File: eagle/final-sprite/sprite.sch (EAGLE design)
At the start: 62 parts, among them J1 M20-7910442R, U1 CC430F513X, U2 LSM9DS1, U4 DRV8837, U5 ADP5092, U6 DRV8837, U7 DRV8837, X1 SPRITEPIN_SPRITE_PIN, X2 SPRITEPIN_SPRITE_PIN

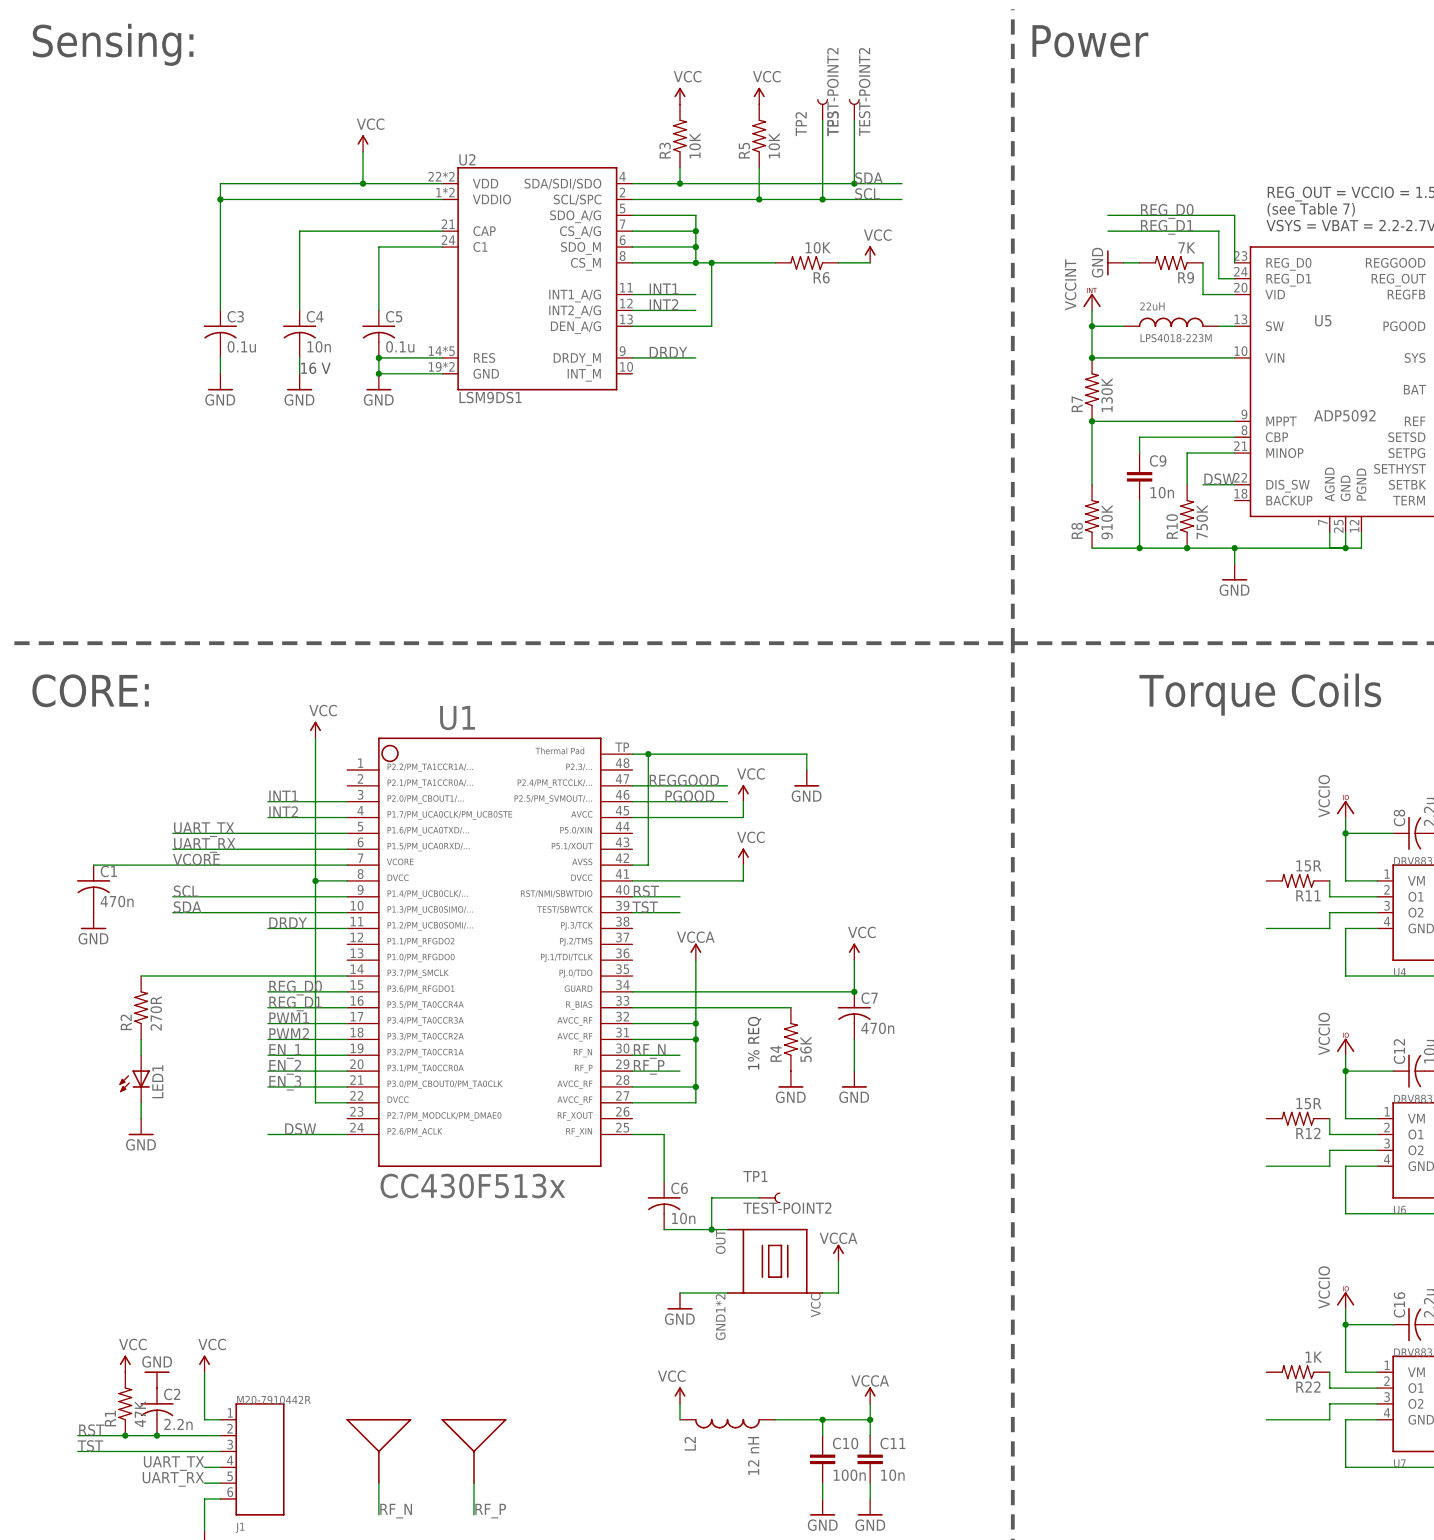
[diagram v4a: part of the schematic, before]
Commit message: started layout and fixed R0402 packages
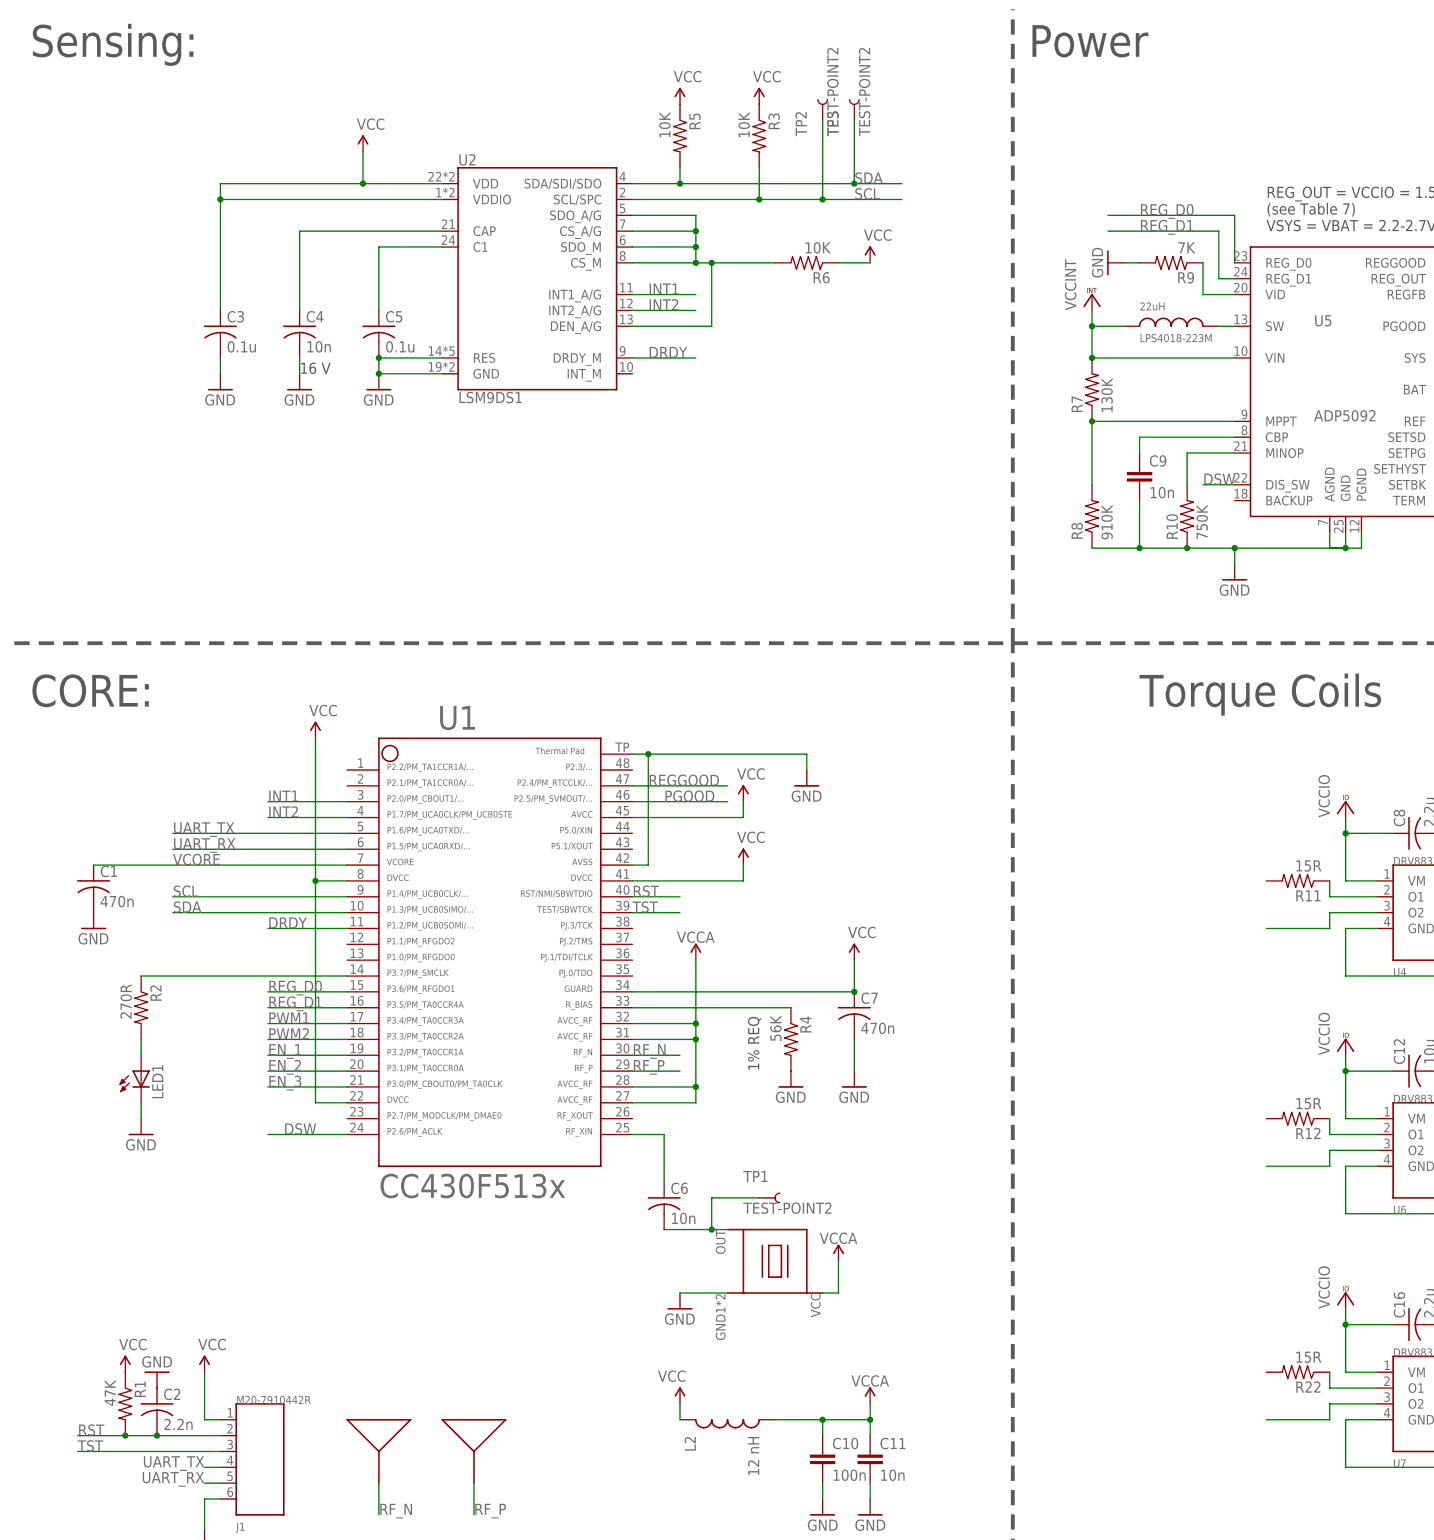
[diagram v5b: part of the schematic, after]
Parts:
- R1, R11, R12, R2, R3, R4, R5, R6: device rcl:R-US_R0402 -> resistor:R-US_R0402
- R22: value 1K -> 15R; device rcl:R-US_R0402 -> resistor:R-US_R0402
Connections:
- net GND: now also R4.2; no longer R4.1
- net N$11: now also R2.2; no longer R2.1
- net N$2: now also R2.1; no longer R2.2
- net N$3: now also R4.1; no longer R4.2
- net RST: now also R1.2; no longer R1.1
- net SCL: now also R3.2; no longer R5.1
- net SDA: now also R5.2; no longer R3.1
- net VCC: now also R1.1, R3.1, R5.1; no longer R1.2, R3.2, R5.2
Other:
- moved on the sheet: R1, R2, R3, R4, R5

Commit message: some schematic updates
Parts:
- added L3, L4: PCBSAT-TORQUECOIL, STAC:PCBSAT-TORQUECOIL
- R18: value 5M -> 5.49M
- R19: value 5M -> 4.53M
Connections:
- new net N$4: L3.P$1, R11.2
- new net N$9: L4.P$1, R12.2
- net N$14: now also L3.P$2
- net N$27: now also L4.P$2
- net N$28: now also R22.2
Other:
- note added: "All Caps 3.3V Except C21 (16V) All Passives 0402 All Passives (5%) Except R4, R15 - R21 (1%) Subject to Change R2, R11, R12, R22 R7, R8 C3 MPPT Max efficiency: R7/(R7 + R8) = 87%"
- note added: "PCB Spiral Inductor Layers 2 and 3"
- note removed: "All Caps 3.3V Except C21 (16V) All Passives 0402 Subject to Change R11, R12, R22 C3"
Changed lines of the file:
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@@
 <part name="R7" library="resistor" library_urn="urn:adsk.eagle:library:348" deviceset="R-US_" device="R0402" package3d_urn="urn:adsk.eagle:package:26058/1" value="130K"/>
 <part name="GND15" library="SparkFun" deviceset="GND" device=""/>
-<part name="R19" library="resistor" library_urn="urn:adsk.eagle:library:348" deviceset="R-US_" device="R0402" package3d_urn="urn:adsk.eagle:package:26058/1" value="5M"/>
+<part name="R19" library="resistor" library_urn="urn:adsk.eagle:library:348" deviceset="R-US_" device="R0402" package3d_urn="urn:adsk.eagle:package:26058/1" value="4.53M"/>
 <part name="R15" library="resistor" library_urn="urn:adsk.eagle:library:348" deviceset="R-US_" device="R0402" package3d_urn="urn:adsk.eagle:package:26058/1"/>
 <part name="R16" library="resistor" library_urn="urn:adsk.eagle:library:348" deviceset="R-US_" device="R0402" package3d_urn="urn:adsk.eagle:package:26058/1"/>
 <part name="R17" library="resistor" library_urn="urn:adsk.eagle:library:348" deviceset="R-US_" device="R0402" package3d_urn="urn:adsk.eagle:package:26058/1"/>
-<part name="R18" library="resistor" library_urn="urn:adsk.eagle:library:348" deviceset="R-US_" device="R0402" package3d_urn="urn:adsk.eagle:package:26058/1" value="5M"/>
+<part name="R18" library="resistor" library_urn="urn:adsk.eagle:library:348" deviceset="R-US_" device="R0402" package3d_urn="urn:adsk.eagle:package:26058/1" value="5.49M"/>
 <part name="L1" library="STAC" deviceset="LPS4018-223M" device=""/>
 <part name="VCC1" library="supply1" library_urn="urn:adsk.eagle:library:371" deviceset="VCCINT" device=""/>
@@
 <part name="R12" library="resistor" library_urn="urn:adsk.eagle:library:348" deviceset="R-US_" device="R0402" package3d_urn="urn:adsk.eagle:package:26058/1" value="15R"/>
 <part name="R22" library="resistor" library_urn="urn:adsk.eagle:library:348" deviceset="R-US_" device="R0402" package3d_urn="urn:adsk.eagle:package:26058/1" value="15R"/>
+<part name="L3" library="STAC" deviceset="PCBSAT-TORQUECOIL" device=""/>
+<part name="L4" library="STAC" deviceset="PCBSAT-TORQUECOIL" device=""/>
 </parts>
 <sheets>
@@
 <text x="-27.94" y="-124.46" size="1.778" layer="97">16 V</text>
 <text x="45.72" y="-236.22" size="1.778" layer="97" rot="R90">1% REQ</text>
-<text x="218.44" y="-215.9" size="3.81" layer="97">All Caps 3.3V
+<text x="223.52" y="-243.84" size="3.81" layer="97">All Caps 3.3V
 Except C21 (16V)
 All Passives 0402
+All Passives (5%)
+Except R4, R15 - R21 (1%)
 Subject to Change
-R11, R12, R22
-C3</text>
+R2, R11, R12, R22
+R7, R8
+C3
+MPPT Max efficiency:
+R7/(R7 + R8) = 87%</text>
 <wire x1="208.28" y1="-297.18" x2="208.28" y2="-167.64" width="0.6096" layer="97" style="longdash"/>
 <text x="215.9" y="-177.8" size="5.08" layer="97">Design Notes</text>
+<wire x1="124.46" y1="-294.64" x2="124.46" y2="-292.1" width="0.1524" layer="97" curve="-180"/>
+<wire x1="124.46" y1="-292.1" x2="124.46" y2="-289.56" width="0.1524" layer="97" curve="-180"/>
+<wire x1="124.46" y1="-289.56" x2="124.46" y2="-287.02" width="0.1524" layer="97" curve="-180"/>
+<wire x1="124.46" y1="-287.02" x2="124.46" y2="-284.48" width="0.1524" layer="97" curve="-180"/>
+<text x="106.68" y="-292.1" size="1.27" layer="97">PCB Spiral Inductor
+Layers 2 and 3</text>
 </plain>
 <instances>
@@
 <instance part="R12" gate="G$1" x="132.08" y="-243.84" rot="R180"/>
 <instance part="R22" gate="G$1" x="132.08" y="-284.48" rot="R180"/>
+<instance part="L3" gate="G$1" x="121.92" y="-210.82" rot="R270"/>
+<instance part="L4" gate="G$1" x="121.92" y="-248.92" rot="R270"/>
 </instances>
 <busses>
@@
 <pinref part="U4" gate="G$1" pin="O2"/>
 <wire x1="144.78" y1="-210.82" x2="137.16" y2="-210.82" width="0.1524" layer="91"/>
-<wire x1="137.16" y1="-210.82" x2="137.16" y2="-213.36" width="0.1524" layer="91"/>
-<wire x1="137.16" y1="-213.36" x2="127" y2="-213.36" width="0.1524" layer="91"/>
+<wire x1="137.16" y1="-210.82" x2="137.16" y2="-215.9" width="0.1524" layer="91"/>
+<wire x1="137.16" y1="-215.9" x2="121.92" y2="-215.9" width="0.1524" layer="91"/>
+<pinref part="L3" gate="G$1" pin="P$2"/>
 </segment>
 </net>
@@
 <pinref part="U6" gate="G$1" pin="O2"/>
 <wire x1="144.78" y1="-248.92" x2="137.16" y2="-248.92" width="0.1524" layer="91"/>
-<wire x1="137.16" y1="-248.92" x2="137.16" y2="-251.46" width="0.1524" layer="91"/>
-<wire x1="137.16" y1="-251.46" x2="127" y2="-251.46" width="0.1524" layer="91"/>
+<wire x1="137.16" y1="-248.92" x2="137.16" y2="-254" width="0.1524" layer="91"/>
+<wire x1="137.16" y1="-254" x2="121.92" y2="-254" width="0.1524" layer="91"/>
+<pinref part="L4" gate="G$1" pin="P$2"/>
 </segment>
 </net>
@@
 <pinref part="U7" gate="G$1" pin="O2"/>
 <wire x1="144.78" y1="-289.56" x2="137.16" y2="-289.56" width="0.1524" layer="91"/>
-<wire x1="137.16" y1="-289.56" x2="137.16" y2="-292.1" width="0.1524" layer="91"/>
-<wire x1="137.16" y1="-292.1" x2="127" y2="-292.1" width="0.1524" layer="91"/>
+<wire x1="137.16" y1="-289.56" x2="137.16" y2="-294.64" width="0.1524" layer="91"/>
+<wire x1="137.16" y1="-294.64" x2="124.46" y2="-294.64" width="0.1524" layer="91"/>
+<pinref part="R22" gate="G$1" pin="2"/>
+<wire x1="127" y1="-284.48" x2="124.46" y2="-284.48" width="0.1524" layer="91"/>
+<wire x1="124.46" y1="-284.48" x2="124.46" y2="-294.64" width="0.1524" layer="91"/>
 </segment>
 </net>
@@
 </segment>
 </net>
+<net name="N$4" class="0">
+<segment>
+<pinref part="L3" gate="G$1" pin="P$1"/>
+<pinref part="R11" gate="G$1" pin="2"/>
+<wire x1="121.92" y1="-205.74" x2="127" y2="-205.74" width="0.1524" layer="91"/>
+</segment>
+</net>
+<net name="N$9" class="0">
+<segment>
+<pinref part="L4" gate="G$1" pin="P$1"/>
+<pinref part="R12" gate="G$1" pin="2"/>
+<wire x1="121.92" y1="-243.84" x2="127" y2="-243.84" width="0.1524" layer="91"/>
+</segment>
+</net>
